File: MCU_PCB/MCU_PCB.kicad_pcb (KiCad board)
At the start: 2 copper layers, 70 x 70 mm, 51 parts, among them J1 BackBone, J2 D1, J3 D2, J4 Micro_SD_Card, J5 CAM_0, J6 CAM_1, J7 47080-4005, U1 STM32G071GBU, U2 MCP795W22-I/ST, U3 74HCT4051BQ-Q100,1, U4 74HCT4051BQ-Q100,1, U5 ADT7310, U6 LIS2MDLTR, U7 LSM6DSRX, Y1 TG-3541CE

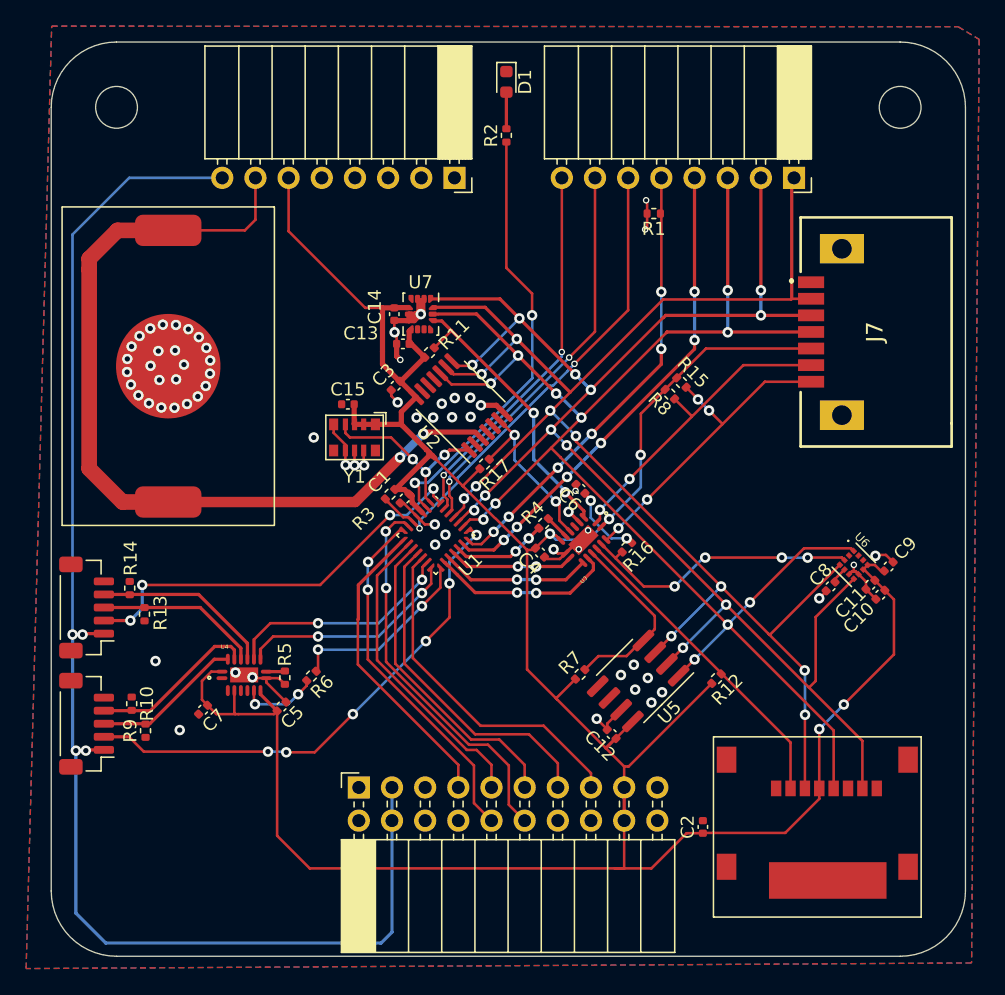
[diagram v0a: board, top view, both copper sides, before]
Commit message: 0.2v KiCad
Improved aesthetics;
More sufficient grounding.
What have to be done:
Traces have to be moved closer and some of the trace widths have to be changed from 0.2 mm to 0.25 mm (especially MCU).
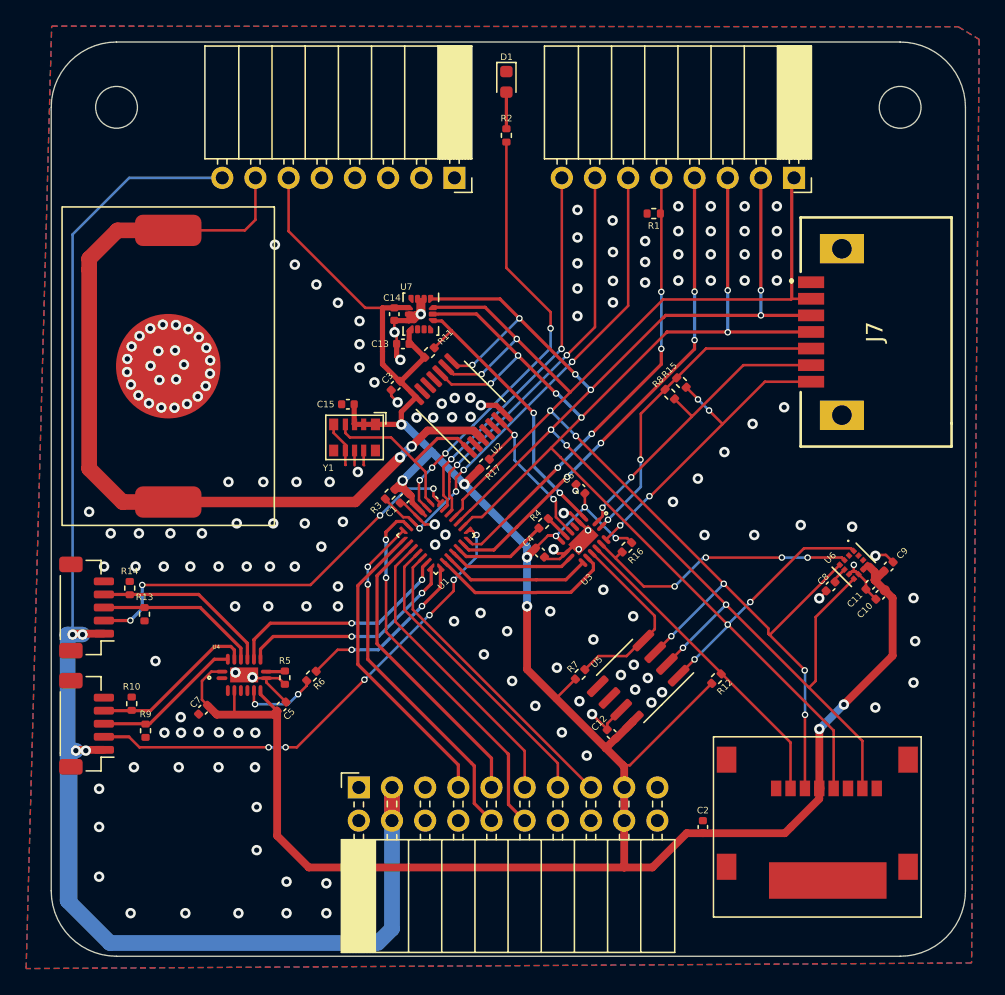
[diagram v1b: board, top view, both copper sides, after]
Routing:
- net +4V: track 107.3 -> 171.3 mm
- net +3V3: track 234.2 -> 290.7 mm, vias 7 -> 12
- net /IO/BUZZER: track 26.4 -> 23.5 mm
- net /IO/ROPE_CUT: track 25.6 -> 23.2 mm
- net /CAM_SENS/HB_0: track 39.2 -> 37.9 mm
- net /IO/ADC_4V: track 24.2 -> 23.0 mm
- net /MCU/OSC32_IN: track 14.6 -> 15.8 mm, vias 3 -> 0
- net /MCU/MUX_EN_1: track 14.6 -> 13.7 mm
- net /IO/COM_TX: track 29.6 -> 28.7 mm
- net +BATT: track 74.6 -> 75.4 mm
- net GND: track 50.9 -> 50.3 mm, vias 66 -> 173
- net /MCU/LED_0: track 33.5 -> 33.9 mm, vias 2 -> 4
- net /CAM_SENS/MOSI: track 115.9 -> 116.1 mm, vias 10 -> 8
- net /CAM_SENS/MISO: track 119.7 -> 119.5 mm, vias 12 -> 10
- net /CAM_SENS/CLK: track 119.5 -> 119.3 mm, vias 11 -> 9
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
